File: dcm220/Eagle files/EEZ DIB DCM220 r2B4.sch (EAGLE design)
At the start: 245 parts, among them IC1 Si8662AB-B-IS1, IC10 MC33272ADR2G, IC11 LT3763EFE#PBF, IC12 MC33274ADR2G, IC13 LT3763EFE#PBF, IC2 TPS54060DGQ, IC3 Si8641AB-B-IS1, IC4 M24C32-WMN6P, IC5 LP2985-33DBVR, IC6 74HC2G04GW,125, IC7 N.C., IC8 STM32F373C8T6, IC9 TL431B, J1 4907, J2 571-0500, J3 571-0100, J4 571-0500, J5 571-0100, Q1 BSP716NH6327XTSA1, Q10 BSS84, Q2 NTD5867NLT4G, Q3 NTD5867NLT4G, Q4 BSS205NH6327XTSA1, Q5 BSS84, Q6 BSP716NH6327XTSA1, Q7 NTD5867NLT4G, Q8 NTD5867NLT4G, Q9 BSS205NH6327XTSA1, X1 172648-0102, X2 77317-104-28LF, X3 N.C., X4 DS1024-2*5R0, Y1 LF XTAL026392

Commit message: DCM220 r2B4
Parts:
- removed R76: 3K6, rcl:R-EU_R0805
- removed R77: 120R, rcl:R-EU_R0805
- removed R78: 11K8, rcl:R-EU_R0805
- removed R79: 15K, rcl:R-EU_R0805
- added D10: N.C., EEZ_Lib1:SCHOTTKYSOD123
- added D11, D9: SKL16, EEZ_Lib1:SCHOTTKYSOD123
- added D12: N.C., EEZ_Lib1:SCHOTTKYSMA_DO-214AC
- C13: value 22u -> N.C.
- C16: value 18p -> 33p
- C22: value 1u -> N.C.
- C55, C75: device rcl:C-EUC1210 -> rcl:C-EUC1206
- D3, D4, D6: value BAW56L -> SKL16; device EEZ_Lib1:BAW56L -> EEZ_Lib1:SCHOTTKYSOD123
- D5: device EEZ_Lib1:SCHOTTKYSMA_DO-214AC -> EEZ_Lib1:SCHOTTKYSOD123
- D7: value BAW56L -> N.C.; device EEZ_Lib1:BAW56L -> EEZ_Lib1:SCHOTTKYSMA_DO-214AC
- D8: value N.C. -> SKL16; device EEZ_Lib1:SCHOTTKYSMA_DO-214AC -> EEZ_Lib1:SCHOTTKYSOD123
- KK1, KK2: value PCB-MB -> PMB-1
- R29: value 330K -> 86K6
- R30, R56: value 22K -> 16K
- R32: value 0R -> 16K
- R33: value 22K -> 10K
- R34: value 10K -> R012/2W; device rcl:R-EU_R0805 -> EEZ_Lib1:R-EU_4WIRE2512
- R35: value R012/2W -> 10R; device EEZ_Lib1:R-EU_4WIRE2512 -> rcl:R-EU_R0805
- R37: value 10R -> N.C.; device rcl:R-EU_R0805 -> rcl:R-EU_R1206
- R38: value 0R -> 2K2
- R39: value N.C. -> 30K; device rcl:R-EU_R1206 -> rcl:R-EU_R0805
- R40, R66: value 2K2 -> 86K6
- R41: value 30K -> 3K3
- R43: value 3K3 -> 47K
- R44, R68: value 86K6 -> 47K
- R45: value 47K -> 30K
- R46: value 47K -> 3K9
- R47: value 30K -> 12K
- R48: value 3K9 -> 3K6
- R49: value 12K -> 120R
- R50: value 3K6 -> 11K8
- R51: value 120R -> 15K
- R52: value 11K8 -> 10R
- R53: value 15K -> 86K6
- R54: value 10R -> 16K
- R55: value 330K -> 10K
- R58: value 0R -> R012/2W; device rcl:R-EU_R0805 -> EEZ_Lib1:R-EU_4WIRE2512
- R59: value 22K -> 10R
- R60: value 10K -> 10R
- R61: value R012/2W -> N.C.; device EEZ_Lib1:R-EU_4WIRE2512 -> rcl:R-EU_R1206
- R62: value 10R -> 2K2
- R63: value 10R -> 30K
- R64: value 0R -> 86K6
- R65: value N.C. -> 3K3; device rcl:R-EU_R1206 -> rcl:R-EU_R0805
- R67: value 30K -> 47K
- R69: value 3K3 -> 30K
- R70: value 86K6 -> 3K9
- R71: value 47K -> 12K
- R72: value 47K -> 3K6
- R73: value 30K -> 120R
- R74: value 3K9 -> 11K8
- R75: value 12K -> 15K
- X1: value 172648-0102 -> 39-30-1020
- ZD2, ZD4: value MM3Z9V1T1G -> MM3Z2V4T1G
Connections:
- removed net N$19: Q2.G, R32.2
- removed net N$2: Q3.G, R38.2
- removed net N$256: Q7.G, R58.2
- removed net N$258: Q8.G, R64.2
- net +8V: now also D10.A, D5.A
- net CC_LED#1: now also R49.2; no longer R51.2
- net CC_LED#2: now also R73.2; no longer R77.2
- net DC_OUT+: now also R52.1, R53.1; no longer R54.1, R55.1
- net DC_OUT-: now also D12.A, D7.A, R37.1, R41.2, R61.1, R65.2; no longer D5.A, D8.A, R39.1, R43.2, R65.1, R69.2
- net FB1: now also R39.1, R46.2; no longer R41.1, R50.2
- net FB2: now also R63.1, R70.2, R72.2; no longer R67.1, R74.2, R76.2
- net GND: now also R33.1, R42.1, R45.1, R46.1, R51.1, R54.1, R57.1, R66.1, R69.1, R71.1; no longer R34.1, R44.1, R48.1, R49.1, R53.1, R56.1, R60.1, R73.1, R74.1, R79.1
- net INTVCC1: now also D6.A, R43.1, R44.2; no longer D4.CA, R45.1, R46.2
- net INTVCC2: now also D11.A, R67.1, R68.2; no longer D7.CA, R71.1, R72.2
- net ISET2: now also R55.2; no longer R57.2
- net I_MON1: now also R38.1; no longer R40.1
- net I_MON2: now also R62.1; no longer R66.1
- net I_SET#1: now also R32.1; no longer R33.1
- net I_SET#2: now also R56.1; no longer R59.1
- net LOUT1: now also R34.1; no longer R35.1
- net LOUT2: now also R58.1; no longer R61.1
- net N$1: now also Q3.G; no longer R38.1
- net N$11: now also R49.1; no longer R51.1
- net N$13: now also R45.2; no longer R47.2
- net N$15: now also Q2.G; no longer R32.1
- net N$16: now also R34.2S, R36.2; no longer R35.2S, R37.2
- net N$17: now also R37.2; no longer R39.2
- net N$18: now also R44.1; no longer R46.1
- net N$22: now also D6.C; no longer D4.K1, D4.K2
- net N$25: now also R73.1; no longer R77.1
- net N$250: now also R32.2; no longer R34.2
- net N$253: now also R68.1; no longer R72.1
- net N$255: now also Q7.G; no longer R58.1
- net N$257: now also Q8.G; no longer R64.1
- net N$26: now also D4.C; no longer D3.K1
- net N$261: now also R58.1S, R59.2; no longer R61.1S, R62.2
- net N$262: now also R58.2S, R60.2; no longer R61.2S, R63.2
- net N$263: now also R61.2; no longer R65.2
- net N$264: now also D11.C; no longer D7.K1, D7.K2
- net N$267: now also R62.2; no longer R66.2
- net N$271: now also R74.1, R75.2; no longer R78.1, R79.2
- net N$278: now also R54.2, R55.1; no longer R56.2, R57.1
- net N$28: now also R66.2; no longer R70.2
- net N$311: now also R56.2, R57.2; no longer R59.2, R60.2
- net N$37: now also R69.2; no longer R73.2
- net N$39: now also D3.C, D5.C; no longer D3.K2
- net N$42: now also D10.C, D8.C; no longer D6.K2
- net N$43: now also D3.A, D4.A; no longer D3.CA
- net N$46: now also D9.C, R53.2; no longer D6.K1, R55.2
- net N$48: now also R38.2; no longer R40.2
- net N$54: now also R50.1, R51.2; no longer R52.1, R53.2
- net N$61: now also D8.A, D9.A; no longer D6.CA
- net N$7: now also R34.1S, R35.2; no longer R35.1S, R36.2
- net N$8: now also R42.2; no longer R44.2
- net PWM#1: now also R43.2; no longer R45.2
- net PWM#2: now also R67.2; no longer R71.2
- net Q6D: now also R52.2; no longer R54.2
- net SENSE1+: now also R35.1; no longer R36.1
- net SENSE1+1: now also R59.1; no longer R62.1
- net SENSE1-: now also R36.1; no longer R37.1
- net SENSE1-1: now also R60.1; no longer R63.1
- net SW1: now also D7.C; no longer D5.C
- net SW2: now also D12.C; no longer D8.C
- net U_MON1: now also R40.1, R47.2; no longer R42.1, R49.2
- net U_MON2: now also R64.1, R71.2; no longer R68.1, R75.2
- net U_SET#1: now also R48.1; no longer R50.1
- net U_SET#2: now also R72.1; no longer R76.1
- net VOUT1+: now also R34.2, R39.2, R40.2; no longer R35.2, R41.2, R42.2
- net VOUT2+: now also R58.2, R63.2, R64.2; no longer R61.2, R67.2, R68.2
- net VOUT_LC1+: now also R41.1; no longer R43.1
- net VOUT_LC2+: now also R65.1; no longer R69.1
- net VREF1: now also R50.2; no longer R52.2
- net VREF2: now also R74.2; no longer R78.2
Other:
- note added: "0 .. +3.3V from PWM"
- note removed: "Glue heatsink ICKSMDB13SA over Q1 and Q2"
- note removed: "Glue heatsink ICKSMDB13SA over Q5 and Q6"
- moved on the sheet: D5, D8, JP1, Q1, Q6, R28, R32, R33, R36, R37, R38, R39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

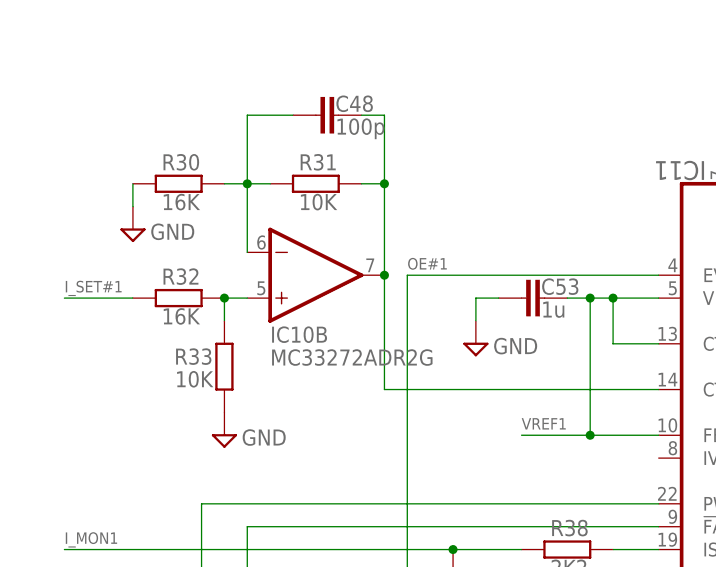
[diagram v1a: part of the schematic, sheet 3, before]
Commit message: DCM220 eagle files
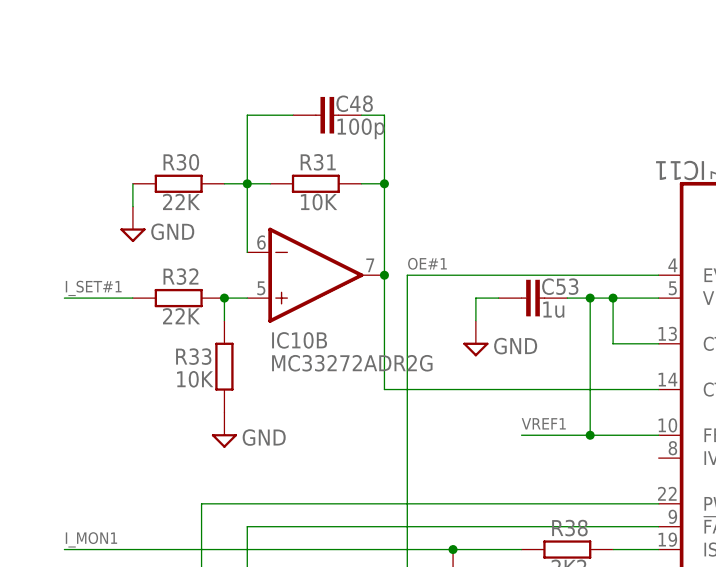
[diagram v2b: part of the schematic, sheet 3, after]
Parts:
- R30, R32, R54, R56: value 16K -> 22K
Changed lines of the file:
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@@
 <part name="IC10" library="EEZ_Lib1" deviceset="TL072" device="SOIC8" value="MC33272ADR2G"/>
 <part name="R31" library="rcl" deviceset="R-EU_" device="R0805" value="10K"/>
-<part name="R30" library="rcl" deviceset="R-EU_" device="R0805" value="16K"/>
+<part name="R30" library="rcl" deviceset="R-EU_" device="R0805" value="22K"/>
 <part name="SUPPLY20" library="supply2" deviceset="GND" device=""/>
 <part name="C45" library="rcl" deviceset="C-EU" device="C0603" value="100n"/>
@@
 <part name="Q9" library="EEZ_Lib1" deviceset="2N7002" device="" value="BSS205NH6327XTSA1"/>
 <part name="R55" library="rcl" deviceset="R-EU_" device="R0805" value="10K"/>
-<part name="R54" library="rcl" deviceset="R-EU_" device="R0805" value="16K"/>
+<part name="R54" library="rcl" deviceset="R-EU_" device="R0805" value="22K"/>
 <part name="SUPPLY30" library="supply2" deviceset="GND" device=""/>
 <part name="C75" library="rcl" deviceset="C-EU" device="C1206" value="22u"/>
@@
 <part name="L4" library="EEZ_inductors_and_transformers" deviceset="125CDMCC/DS" device="" value="125CDMCCDS-330MC"/>
 <part name="R33" library="rcl" deviceset="R-EU_" device="R0805" value="10K"/>
-<part name="R32" library="rcl" deviceset="R-EU_" device="R0805" value="16K"/>
+<part name="R32" library="rcl" deviceset="R-EU_" device="R0805" value="22K"/>
 <part name="SUPPLY18" library="supply2" deviceset="GND" device=""/>
 <part name="R57" library="rcl" deviceset="R-EU_" device="R0805" value="10K"/>
-<part name="R56" library="rcl" deviceset="R-EU_" device="R0805" value="16K"/>
+<part name="R56" library="rcl" deviceset="R-EU_" device="R0805" value="22K"/>
 <part name="SUPPLY19" library="supply2" deviceset="GND" device=""/>
 <part name="GND" library="EEZ_connectors" deviceset="TEST-PIN" device="_0.9MM"/>
@@
 </instance>
 <instance part="IC10" gate="B" x="35.56" y="137.16" smashed="yes" rot="MR180">
-<attribute name="NAME" x="30.48" y="131.445" size="1.778" layer="95" rot="MR180"/>
-<attribute name="VALUE" x="30.48" y="128.905" size="1.778" layer="96" rot="MR180"/>
+<attribute name="NAME" x="30.48" y="130.81" size="1.778" layer="95" rot="MR180"/>
+<attribute name="VALUE" x="30.48" y="128.27" size="1.778" layer="96" rot="MR180"/>
 </instance>
 <instance part="GND" gate="G$1" x="170.18" y="165.1" smashed="yes" rot="R90">

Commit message: DCM220 r2B4 .ioc
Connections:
- net N$481: now also OE#2.1; no longer OE#1.1
- net N$482: now also OE#1.1; no longer OE#2.1
- net OE#1: now also OE#1.2; no longer OE#2.2
- net OE#2: now also OE#2.2; no longer OE#1.2
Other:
- moved on the sheet: OE#1, OE#2
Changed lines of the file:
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@@
 <part name="I_SET2" library="EEZ_Lib1" deviceset="JP2-NOCUT" device=""/>
 <part name="U_SET2" library="EEZ_Lib1" deviceset="JP2-NOCUT" device=""/>
+<part name="OE#2" library="EEZ_Lib1" deviceset="JP2-NOCUT" device=""/>
 <part name="OE#1" library="EEZ_Lib1" deviceset="JP2-NOCUT" device=""/>
-<part name="OE#2" library="EEZ_Lib1" deviceset="JP2-NOCUT" device=""/>
 <part name="R43" library="rcl" deviceset="R-EU_" device="R0805" value="47K"/>
 <part name="R67" library="rcl" deviceset="R-EU_" device="R0805" value="47K"/>
@@
 <attribute name="NAME" x="20.32" y="135.255" size="1.27" layer="95" rot="MR0"/>
 </instance>
-<instance part="OE#1" gate="G$1" x="152.4" y="144.78" smashed="yes" rot="R90">
+<instance part="OE#2" gate="G$1" x="152.4" y="144.78" smashed="yes" rot="R90">
 <attribute name="NAME" x="151.765" y="144.78" size="1.27" layer="95" rot="MR270"/>
 </instance>
-<instance part="OE#2" gate="G$1" x="154.94" y="144.78" smashed="yes" rot="R90">
+<instance part="OE#1" gate="G$1" x="154.94" y="144.78" smashed="yes" rot="R90">
 <attribute name="NAME" x="154.305" y="144.78" size="1.27" layer="95" rot="MR270"/>
 </instance>
@@
 <net name="OE#1" class="0">
 <segment>
-<pinref part="OE#2" gate="G$1" pin="2"/>
+<pinref part="OE#1" gate="G$1" pin="2"/>
 <wire x1="154.94" y1="147.32" x2="154.94" y2="154.94" width="0.1524" layer="91"/>
 <label x="154.305" y="150.495" size="1.27" layer="102" rot="R90"/>
@@
 <net name="OE#2" class="0">
 <segment>
-<pinref part="OE#1" gate="G$1" pin="2"/>
+<pinref part="OE#2" gate="G$1" pin="2"/>
 <wire x1="152.4" y1="147.32" x2="152.4" y2="154.94" width="0.1524" layer="91"/>
 <label x="151.765" y="150.495" size="1.27" layer="102" rot="R90"/>
@@
 <net name="N$481" class="0">
 <segment>
-<pinref part="OE#1" gate="G$1" pin="1"/>
+<pinref part="OE#2" gate="G$1" pin="1"/>
 <pinref part="IC8" gate="G$1" pin="PB6"/>
 <wire x1="152.4" y1="144.78" x2="152.4" y2="127" width="0.1524" layer="91"/>
@@
 <net name="N$482" class="0">
 <segment>
-<pinref part="OE#2" gate="G$1" pin="1"/>
+<pinref part="OE#1" gate="G$1" pin="1"/>
 <pinref part="IC8" gate="G$1" pin="PB5"/>
 <wire x1="154.94" y1="144.78" x2="154.94" y2="127" width="0.1524" layer="91"/>
